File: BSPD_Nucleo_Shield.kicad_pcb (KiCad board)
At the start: 2 copper layers, 68.6 x 53.3 mm, 35 parts, among them J1 Conn_01x03, J2 Conn_01x02, J3 Conn_01x02, J4 Digital/PWM, J5 Power, J6 Digital/PWM, J7 Analog, J8 Conn_01x03, Q1 IRFB4110, U1 LM2596S-ADJ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

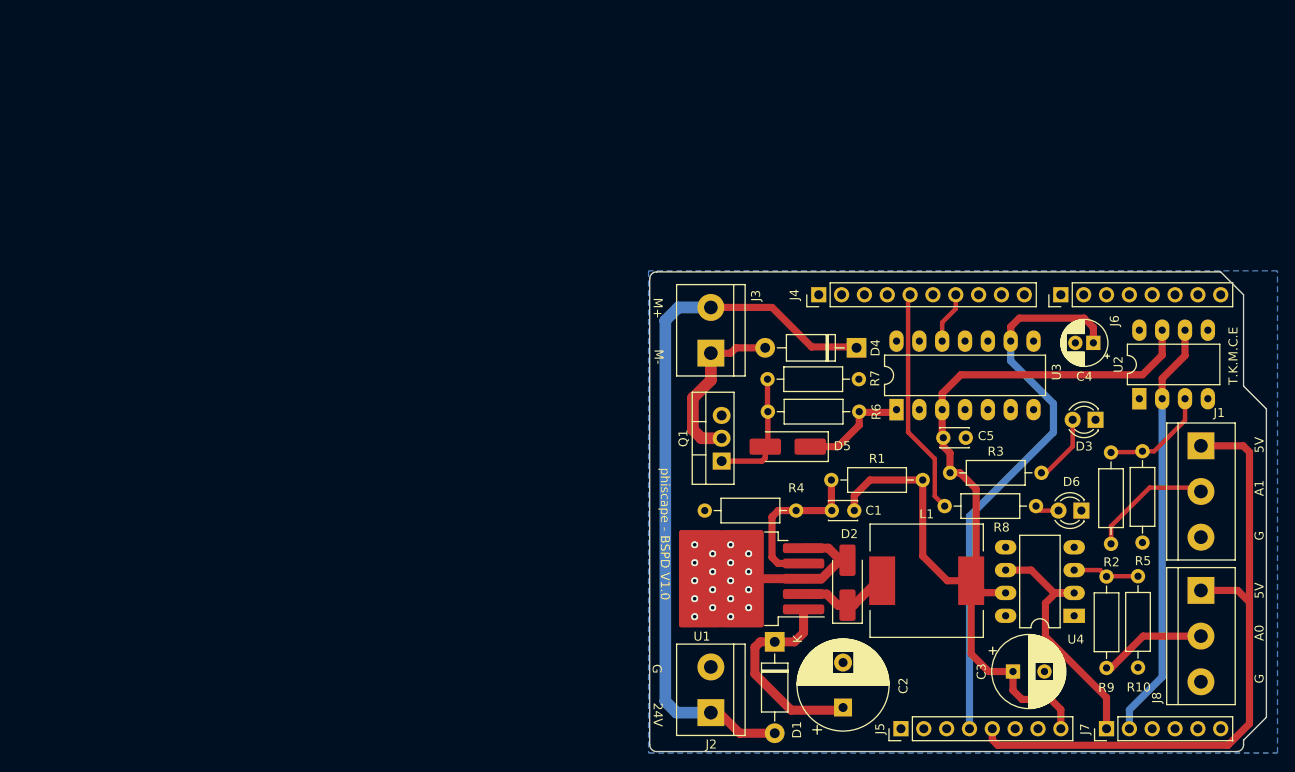
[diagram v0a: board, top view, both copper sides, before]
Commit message: updated to kicad8.0.1
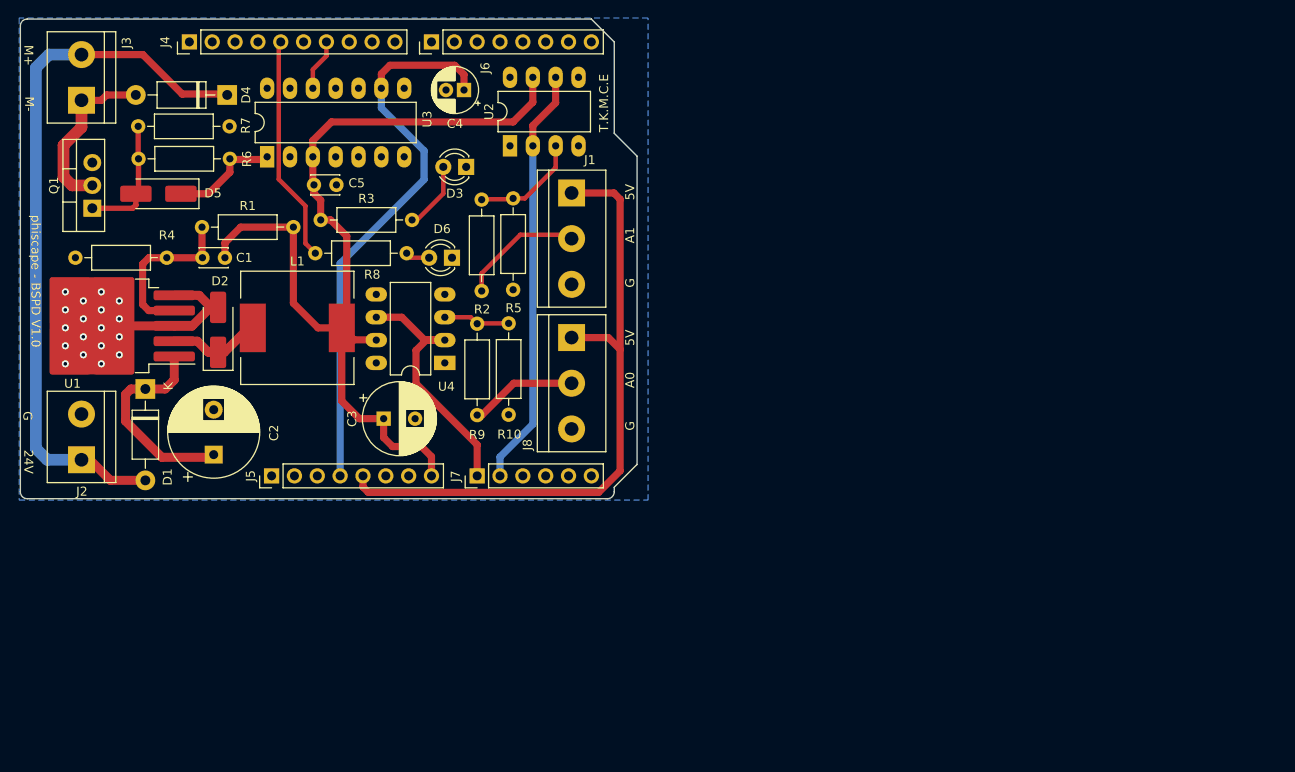
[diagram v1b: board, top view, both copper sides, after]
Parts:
- moved C1 75.4 mm to (50.3, 45.1)
- moved C2 75.4 mm to (51.5, 67.0)
- moved C3 75.4 mm to (70.4, 63.0)
- moved C4 75.4 mm to (79.3, 26.4)
- moved C5 75.4 mm to (65.2, 37.0)
- moved D1 75.4 mm to (43.9, 59.7)
- moved D3 75.4 mm to (79.6, 35.0)
- moved D4 75.4 mm to (53.0, 27.0)
- moved D5 75.4 mm to (45.4, 38.0)
- moved D6 75.4 mm to (78.0, 45.1)
- moved J1 75.4 mm to (91.3, 37.9)
- moved J2 75.4 mm to (36.8, 67.5)
- moved J4 75.4 mm to (48.8, 21.1)
- moved J6 75.4 mm to (75.7, 21.1)
- moved J7 75.4 mm to (80.8, 69.3)
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
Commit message: v1.0 released
placed order for 5 from lion circuits
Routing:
- net /24V_PWR: track 79.7 -> 133.3 mm
